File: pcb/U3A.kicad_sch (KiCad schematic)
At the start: 38 parts, among them J1 Conn_01x03_Pin, J2 Conn_01x07_Pin, J3 USB_C, J4 Conn_01x08_Pin, Q1 AO3401A, SW1 SW_DIP_x02, U1 LD1117S33TR, U2 FT232RL

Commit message: Fix wrong vendor-id of device
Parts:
- R3, R4: VendorId 103195 -> 102962
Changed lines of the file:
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@@
       (effects (font (size 1.27 1.27)) hide)
     )
-    (property "VendorId" "103195" (at 85.09 88.9 0)
+    (property "VendorId" "102962" (at 85.09 88.9 0)
       (effects (font (size 1.27 1.27)) hide)
     )
@@
       (effects (font (size 1.27 1.27)) hide)
     )
-    (property "VendorId" "103195" (at 85.09 91.44 0)
+    (property "VendorId" "102962" (at 85.09 91.44 0)
       (effects (font (size 1.27 1.27)) hide)
     )

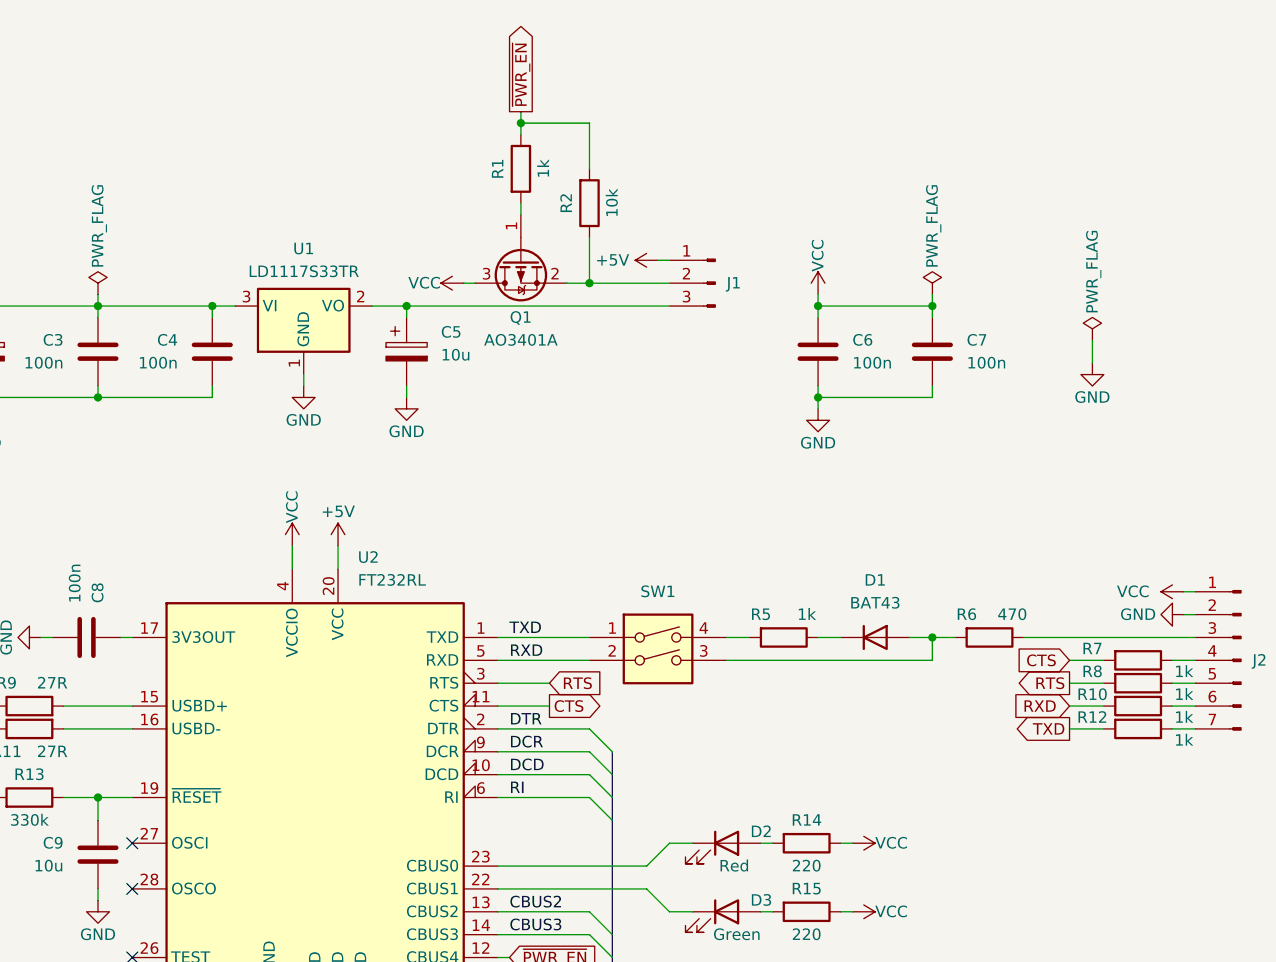
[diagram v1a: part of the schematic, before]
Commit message: Fix voltage error on startup
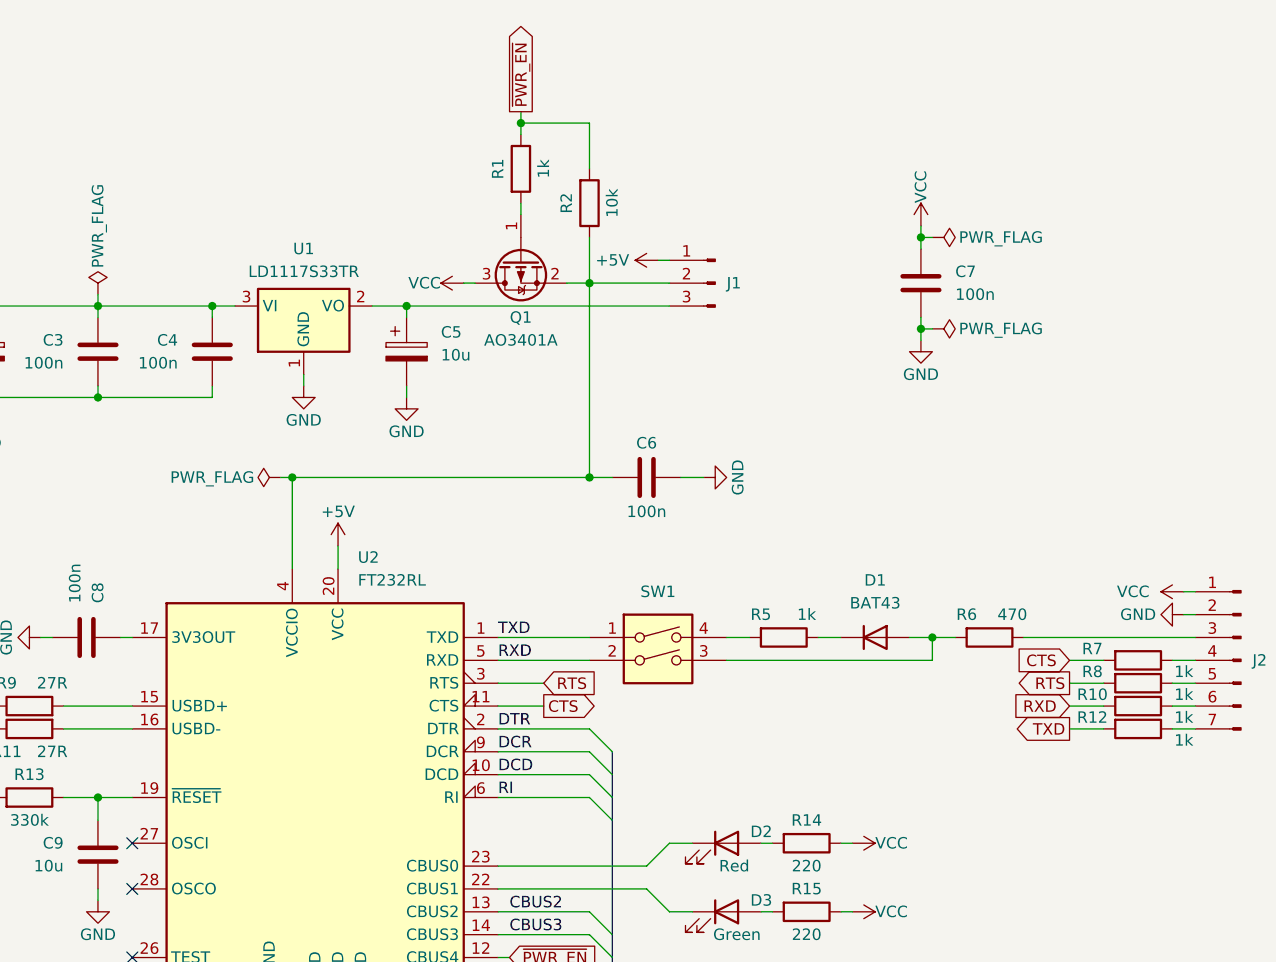
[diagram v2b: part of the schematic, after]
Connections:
- net VCC: no longer C6.2, U2.4 (VCCIO)
- net at J1.2 (Pin_2), Q1.2 (S), R2.1: now also C6.2, U2.4 (VCCIO)
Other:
- moved on the sheet: C6, C7

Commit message: Update to KiCAD 9
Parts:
- H1, H2: now left out of the parts list

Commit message: Rename/Add/Remove bom fields
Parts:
- C1: HTL (none) -> 102538; Vendor HTL -> (none); VendorId 102538 -> (none)
- C2, C5: HTL (none) -> 100140; Vendor HTL -> (none); VendorId 100140 -> (none)
- C3, C4, C6, C7, C8: HTL (none) -> 100128; Vendor HTL -> (none); VendorId 100128 -> (none)
- C9: HTL (none) -> 100138; Vendor HTL -> (none); VendorId 100138 -> (none)
- D1: HTL (none) -> 100205; Vendor HTL -> (none); VendorId 100205 -> (none)
- D2: HTL (none) -> 100458; Vendor HTL -> (none); VendorId 100458 -> (none)
- D3: HTL (none) -> 100459; Vendor HTL -> (none); VendorId 100459 -> (none)
- FB1: HTL (none) -> 103570; Vendor HTL -> (none); VendorId 103570 -> (none)
- J1, J2, J4: HTL (none) -> 101521; Vendor HTL -> (none); VendorId 101521 -> (none)
- J3: HTL (none) -> 103572; Vendor HTL -> (none); VendorId 103572 -> (none)
- Q1: HTL (none) -> 103513; Vendor HTL -> (none); VendorId 103513 -> (none)
- R1, R10, R12, R5, R7, R8: HTL (none) -> 102951; Vendor HTL -> (none); VendorId 102951 -> (none)
- R11, R9: HTL (none) -> 102920; Vendor HTL -> (none); VendorId 102920 -> (none)
- R13: HTL (none) -> 102993; Vendor HTL -> (none); VendorId 102993 -> (none)
- R14, R15: HTL (none) -> 102937; Vendor HTL -> (none); VendorId 102937 -> (none)
- R2: HTL (none) -> 102967; Vendor HTL -> (none); VendorId 102967 -> (none)
- R3, R4: HTL (none) -> 102962; Vendor HTL -> (none); VendorId 102962 -> (none)
- R6: HTL (none) -> 102944; Vendor HTL -> (none); VendorId 102944 -> (none)
- SW1: HTL (none) -> 103604; Vendor HTL -> (none); VendorId 103604 -> (none)
- U1: HTL (none) -> 103444; Vendor HTL -> (none); VendorId 103444 -> (none)
- U2: HTL (none) -> 103271; Vendor HTL -> (none); VendorId 103271 -> (none)
